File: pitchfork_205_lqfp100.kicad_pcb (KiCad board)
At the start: 2 copper layers, 95 x 32 mm, 82 parts, among them P1 SD_CARD, P7 USB-MINI-B, SW1 SW_PUSH, SW2 SW_PUSH, SW3 SW_PUSH, SW4 SW_PUSH, U1 STM32F205Vxx, U2 NRF24L01+, U3 MCP73833, U6 LP38691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

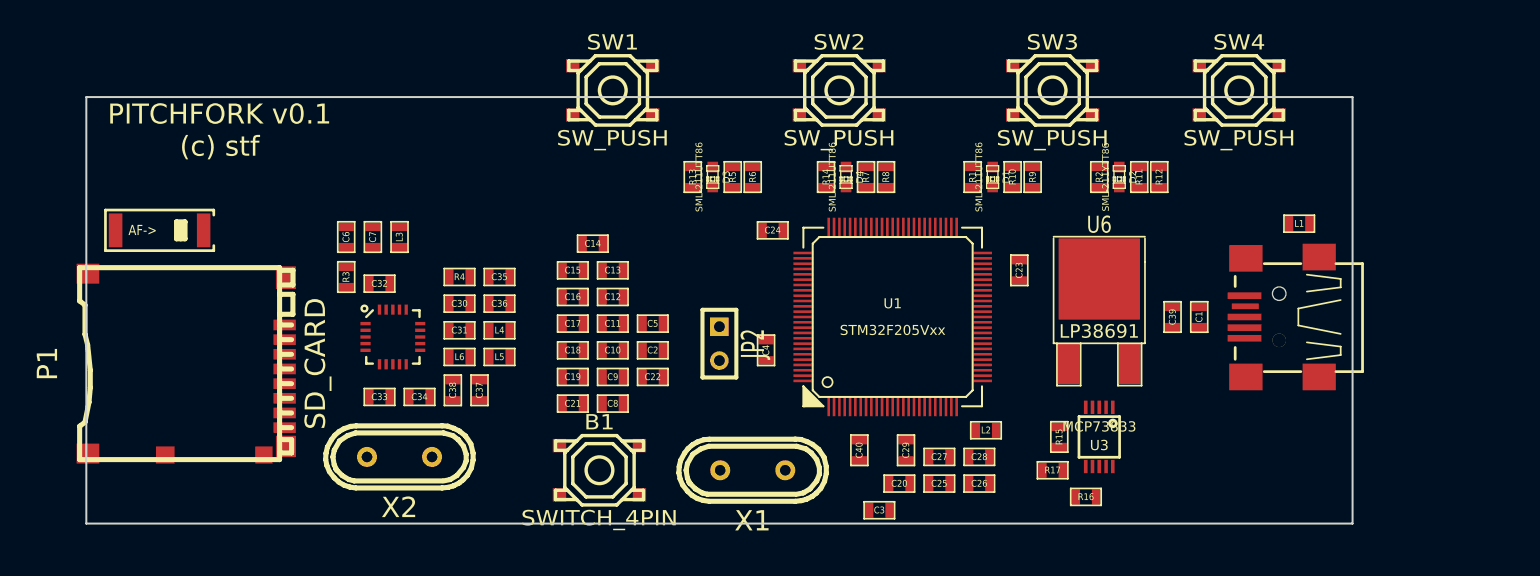
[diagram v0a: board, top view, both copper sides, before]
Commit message: [enh] 1st review, traces drawn
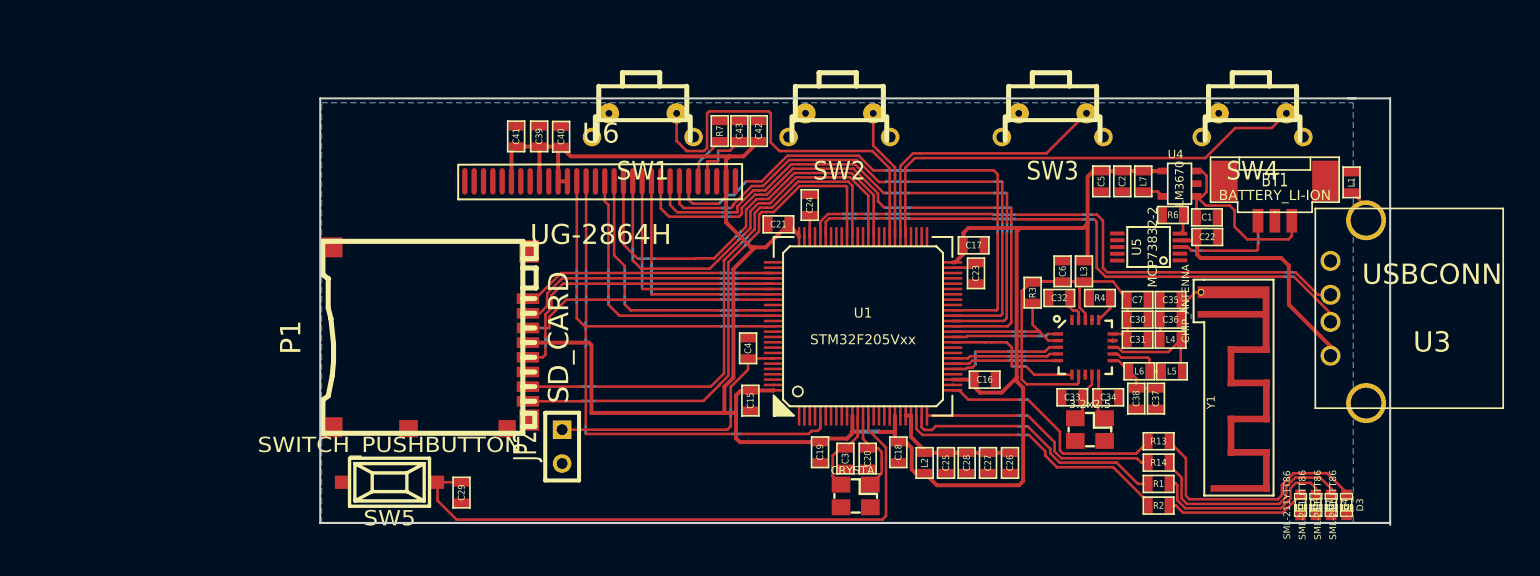
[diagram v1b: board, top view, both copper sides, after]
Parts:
- removed B1: SWITCH_4PIN, smd_push2
- removed C10, C11, C12, C13, C14, C8, C9: 100n, SM0603
- removed P7: USB-MINI-B, CONN_USB2_MiniB_SMT
- removed R10, R12, R8: 47k, SM0603
- removed R11, R5, R9: 1k, SM0603
- removed R15: 2.2k, SM0603
- removed R16: R, SM0603
- removed R17: 150k, SM0603
- added BT1: BATTERY_LI-ION, CONN3_SMD, F.Cu at (244.7, 189.8)
- added C41: 2.2uF, SM0603, F.Cu at (187.8, 186.9)
- added C42: 0.1uF, SM0603, F.Cu at (205.9, 186.6)
- added C43: 2.2uF, SM0603, F.Cu at (204.5, 186.6)
- added L7: 10uH, SM0603, F.Cu at (234.8, 190.3)
- added SW5: SWITCH_PUSHBUTTON, smd_push, F.Cu at (178.2, 212.9)
- added U4: LM3670, SOT23-5, F.Cu at (237.5, 190.5)
- added U5: MCP73832-2, MSOP-10, F.Cu at (235.2, 195.2)
- C1: value 2.2u -> 4.7uF
- C2: value 2.2u -> 10uF
- C22: value 100n -> 10uF
- C39: value 10uF -> 2.2uF
- C40: value 10uF -> 0.1uF
- R6: value 47k -> 2k
- R7: value 1k -> 560k
- SW1, SW2, SW3, SW4: footprint smd_push2 -> MINIBUTVERT
- U3: value MCP73833 -> USBCONN; footprint MSOP10-0.5 -> USB_A
- U6: value LP38691 -> UG-2864H; footprint DPAK2 -> UG-2864H
- X1, X2: footprint Crystal_HC49-U_Vertical_RevA_09Aug2010 -> Crystal_3.2x2.5mm
- Y1: footprint Chip_Antenna_AF_2.4GHz -> Antenna_Meander_2.4GHz_TI_AN043
- moved Y1 78.6 mm to (239.4, 200.3), turned to 270 degrees
- moved C7 57.6 mm to (234.4, 199.2), turned to 180 degrees
- moved C6 53.8 mm to (228.8, 197.1)
- moved D3 53.5 mm to (250.1, 214.6)
- moved C33 52.0 mm to (229.5, 206.5), turned to 180 degrees
- moved U2 52.0 mm to (230.4, 202.8)
- moved X2 51.8 mm to (230.8, 208.9)
- moved C34 51.7 mm to (232.2, 206.5), turned to 0 degrees
- moved R3 51.5 mm to (226.5, 198.7)
- moved L3 51.4 mm to (230.3, 197.1)
- moved C38 51.3 mm to (234.3, 206.6)
- moved C32 51.0 mm to (228.5, 199.1)
- moved L6 51.0 mm to (234.5, 204.6)
- moved C30 50.9 mm to (234.4, 200.7)
- moved C31 50.9 mm to (234.4, 202.2)
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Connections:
- C1 pad 1: +5V -> /+3.7V
- C22 pad 1: +3.3V -> +5V
- C39 pad 1: +5V -> +3.3V
- C40 pad 1: GND -> +3.3V
- C40 pad 2: /VBAT -> GND
- L1 pad 1: GND -> N-0000079
- L1 pad 2: N-0000046 -> GND
- P1 pad 1: /sd_d3 -> /sd_d2
- P1 pad 2: /sd_cmd -> /sd_d3
- P1 pad 3: GND -> /sd_cmd
- R6 pad 1: N-00000108 -> N-00000101
- R7 pad 1: N-00000109 -> N-0000012
- R7 pad 2: /btn1 -> GND
- SW1 pad 1: +3.3V -> /btn0
- SW1 pad 2: N-00000108 -> GND
- SW2 pad 1: +3.3V -> /btn1
- SW2 pad 2: N-00000109 -> GND
- SW3 pad 1: +3.3V -> /btn2
- SW3 pad 2: N-000007 (its old number) -> GND
- SW4 pad 1: +3.3V -> /btn3
- SW4 pad 2: N-000009 -> GND
- U1 pad 23: (no net) -> /led_status
- U1 pad 24: (no net) -> /led_mode
- U1 pad 25: (no net) -> /led_write
- U1 pad 26: (no net) -> /led_read
- U1 pad 35: (no net) -> /nrf_irq
- U1 pad 36: (no net) -> /nrf_ce
- U1 pad 37: (no net) -> /nrf_csn
- U1 pad 38: (no net) -> /lcd_d4
- U1 pad 39: (no net) -> /lcd_d5
- U1 pad 40: (no net) -> /lcd_d6
- U1 pad 41: (no net) -> /lcd_d7
- U1 pad 5: (no net) -> /lcd_res
- U1 pad 52: /nrf_ce -> (no net)
- U1 pad 53: /nrf_irq -> (no net)
- U1 pad 54: /nrf_csn -> (no net)
- U1 pad 59: /led_status -> (no net)
- U1 pad 6: /VBAT -> (no net)
- U1 pad 60: /led_mode -> (no net)
- U1 pad 61: /led_write -> /lcd_d0
- U1 pad 62: /led_read -> /lcd_d1
- U1 pad 69: /usb_id -> (no net)
- U1 pad 81: (no net) -> /lcd_d2
- U1 pad 82: (no net) -> /lcd_d3
- U1 pad 85: (no net) -> /lcd_rd
- U1 pad 86: (no net) -> /lcd_w
- U1 pad 88: (no net) -> /lcd_cs
- U3 pad 2: +5V -> /usb_dm
- U3 pad 3: (no net) -> /usb_dp
- U3 pad 4: (no net) -> GND
- U3 pad 5: GND -> N-0000079
- U3 pad 6: N-000001 (its old number) -> (no net)
- U6 pad 1: +3.3V -> (no net)
- U6 pad 2: GND -> (no net)
- U6 pad 3: +5V -> (no net)
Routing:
- net +3.3V: track 0.00 -> 161.9 mm, vias 0 -> 3
- net /nrst: track 0.00 -> 45.6 mm
- net /lcd_d4: track 0.00 -> 45.1 mm, vias 0 -> 8
- net /usb_dm: track 0.00 -> 44.7 mm, vias 0 -> 12
- net /usb_dp: track 0.00 -> 44.3 mm, vias 0 -> 12
- net /lcd_d5: track 0.00 -> 43.5 mm, vias 0 -> 8
- net /lcd_d6: track 0.00 -> 42.0 mm, vias 0 -> 8
- net /sd_d0: track 0.00 -> 40.5 mm, vias 0 -> 4
- net /lcd_d7: track 0.00 -> 40.3 mm, vias 0 -> 6
- net /sd_d1: track 0.00 -> 40.1 mm, vias 0 -> 4
- net /lcd_res: track 0.00 -> 37.7 mm, vias 0 -> 12
- net /btn3: track 0.00 -> 35.5 mm
- net N-000001: track 0.00 -> 32.5 mm
- net /lcd_d0: track 0.00 -> 31.2 mm, vias 0 -> 4
- net /lcd_d1: track 0.00 -> 31.1 mm, vias 0 -> 4
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- added copper zone on B.Cu, net GND
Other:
- board size 95 x 32 mm -> 80.3 x 32 mm
- net class Default: clearance 0.2 -> 0.1; trace_width 0.254 -> 0.2; via_dia 0.889 -> 0.0295; via_drill 0.635 -> 0.0197
- net class power added: clearance 0.1, trace_width 0.3, via_dia 0.0295, via_drill 0.0197
- rule trace_clearance: 0.2 -> 0.1
- rule trace_min: 0.254 -> 0.008
- rule via_min_drill: 0.508 -> 0.0197
- rule via_min_size: 0.889 -> 0.0295
- board text removed: "PITCHFORK v0.1 (c) stf"

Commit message: [enh] finished backloading sd version
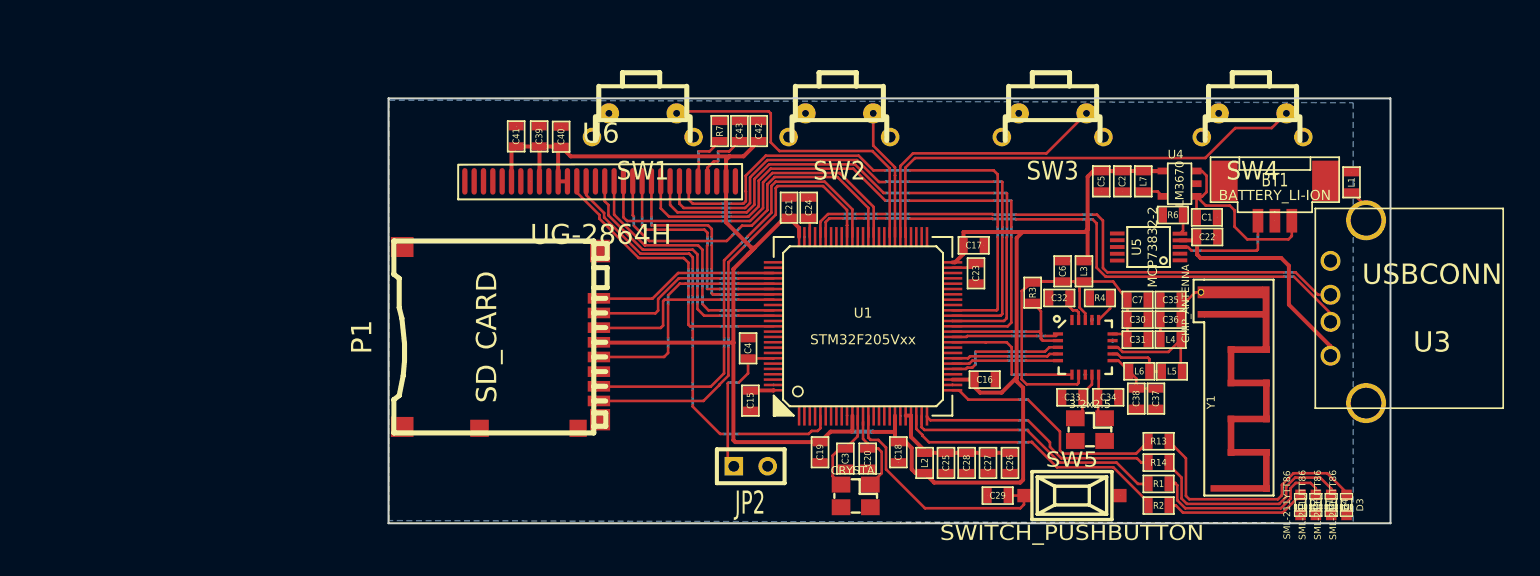
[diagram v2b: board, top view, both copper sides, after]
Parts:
- moved SW5 51.2 mm to (229.4, 213.9), turned to 0 degrees
- moved C29 40.2 mm to (223.9, 213.9), turned to 0 degrees
- moved JP2 14.2 mm to (205.3, 211.7), turned to 0 degrees
- moved P1 5.33 mm to (186.6, 202.0)
- moved C21 1.48 mm to (208.2, 192.3), turned to 270 degrees
- moved C24 0.21 mm to (209.7, 192.3)
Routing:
- net /nrst: track 45.6 -> 18.5 mm
- net +3.3V: track 161.9 -> 149.8 mm
- net /boot0: track 20.3 -> 11.3 mm
- net /sd_d1: track 40.1 -> 34.4 mm
- net /sd_d3: track 20.1 -> 14.7 mm
- net /sd_d2: track 19.2 -> 13.9 mm
- net /sd_d0: track 40.5 -> 35.3 mm
- net /sd_clk: track 23.1 -> 18.0 mm, vias 4 -> 6
- net /btn0: track 29.4 -> 24.3 mm
- net /sd_cmd: track 19.8 -> 15.1 mm, vias 4 -> 2
- net /lcd_res: track 37.7 -> 33.9 mm, vias 12 -> 14
- net /lcd_d0: track 31.2 -> 27.5 mm, vias 4 -> 2
- net /lcd_d1: track 31.1 -> 27.7 mm
- net /lcd_cs: track 25.3 -> 22.6 mm
- net /lcd_d3: track 17.7 -> 19.5 mm, vias 4 -> 8
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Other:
- board size 80.3 x 32 mm -> 75.2 x 31.9 mm
